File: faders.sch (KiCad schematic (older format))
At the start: 11 parts

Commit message: Sub boards completed
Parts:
- added U6: CD74HC4067M, Package_SO:SOIC-24W_7.5x15.4mm_P1.27mm, symbol 74xx:CD74HC4067M
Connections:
- net +5V: now also U6.24 (VCC)
- net GND: now also U6.12 (GND), U6.15 (~E)
- net F_CHAN_1: no longer names the net of RV1.2, SW_F1.20
- net F_CHAN_1: now also U6.9 (I0)
- net F_CHAN_2: no longer names the net of RV2.2, SW_F1.19
- net F_CHAN_2: now also U6.8 (I1)
- net F_CHAN_3: no longer names the net of RV3.2, SW_F1.18
- net F_CHAN_3: now also U6.7 (I2)
- net F_CHAN_4: no longer names the net of RV4.2, SW_F1.17
- net F_CHAN_4: now also U6.6 (I3)
- net F_CHAN_5: no longer names the net of RV5.2, SW_F1.16
- net F_CHAN_5: now also U6.5 (I4)
- net F_CHAN_6: no longer names the net of RV6.2, SW_F1.15
- net F_CHAN_6: now also U6.4 (I5)
- net F_CHAN_7: no longer names the net of RV7.2, SW_F1.14
- net F_CHAN_7: now also U6.3 (I6)
- net F_CHAN_8: no longer names the net of RV8.2, SW_F1.13
- net F_CHAN_8: now also U6.2 (I7)
- net F_MASTER: no longer names the net of RVM1.2, SW_F1.12
- net F_MASTER: now also U6.23 (I8)
- new net FADERS: U6.1 (COM)
- new net S0: U6.10 (S0)
- new net S1: U6.11 (S1)
- new net S2: U6.14 (S2)
- new net S3: U6.13 (S3)
- no-connect marks 2 -> 9
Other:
- moved on the sheet: RN1, RV1, RV2, RV3, RV4, RV5, RV6, RV7, RV8, RVM1, SW_F1

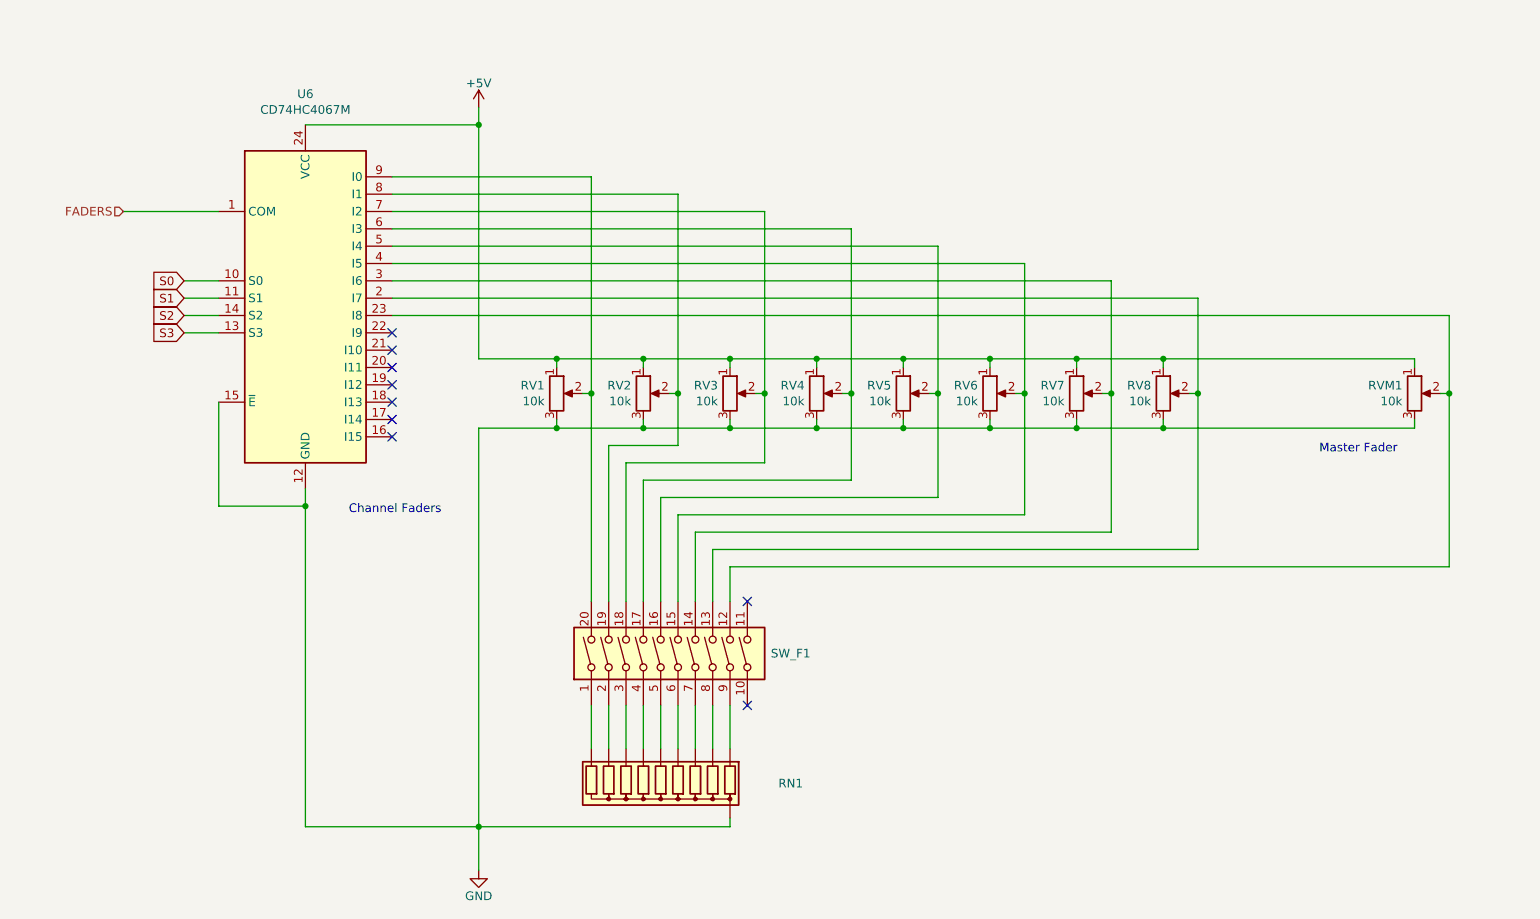
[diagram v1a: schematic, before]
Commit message: Tidy schematic / renumber components / complete daughter boards
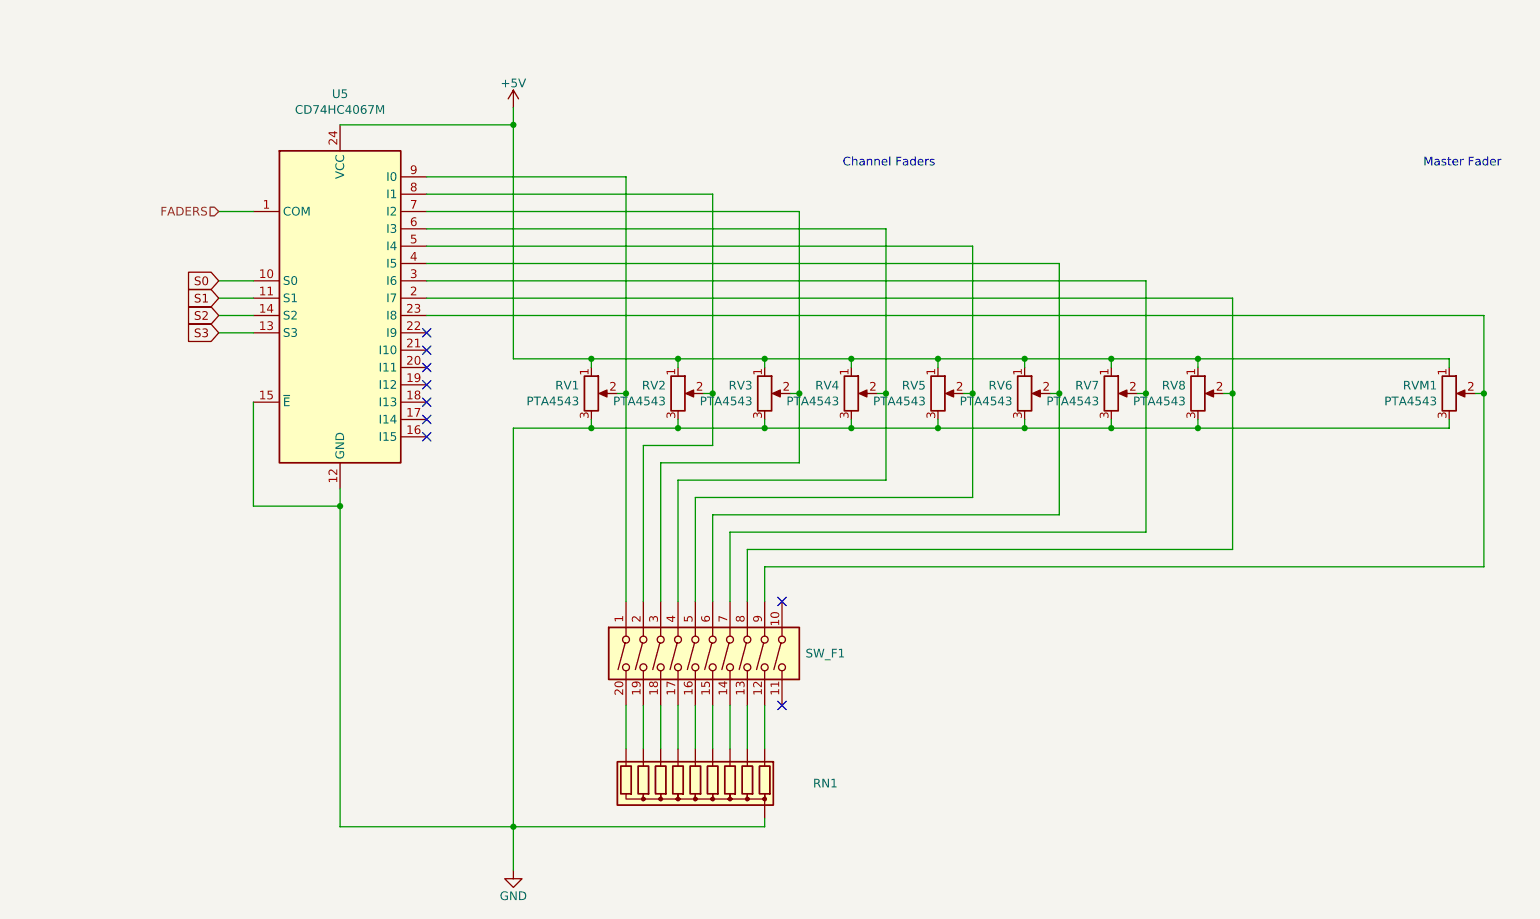
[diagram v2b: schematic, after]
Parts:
- RN1: value R_Network09 -> 2.2K (Bussed)
- RV1, RV2, RV3, RV4, RV5, RV6, RV7, RV8, RVM1: value 10k -> PTA4543
- renumbered U6 to U5
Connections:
- net at SW_F1.1: now also RV1.2, U5.9 (I0); no longer RN1.10 (R9)
- net at RVM1.2, U5.23 (I8): now also SW_F1.9; no longer SW_F1.12
- net at RV8.2, U5.2 (I7): now also SW_F1.8; no longer SW_F1.13
- net at RV7.2, U5.3 (I6): now also SW_F1.7; no longer SW_F1.14
- net at RV6.2, U5.4 (I5): now also SW_F1.6; no longer SW_F1.15
- net at RV5.2, U5.5 (I4): now also SW_F1.5; no longer SW_F1.16
- net at RV4.2, U5.6 (I3): now also SW_F1.4; no longer SW_F1.17
- net at RV3.2, U5.7 (I2): now also SW_F1.3; no longer SW_F1.18
- net at RV2.2, U5.8 (I1): now also SW_F1.2; no longer SW_F1.19
- net at RN1.9 (R8): now also SW_F1.19; no longer SW_F1.2
- net at RN1.8 (R7): now also SW_F1.18; no longer SW_F1.3
- net at RN1.7 (R6): now also SW_F1.17; no longer SW_F1.4
- net at RN1.6 (R5): now also SW_F1.16; no longer SW_F1.5
- net at RN1.5 (R4): now also SW_F1.15; no longer SW_F1.6
- net at RN1.4 (R3): now also SW_F1.14; no longer SW_F1.7
- net at RN1.3 (R2): now also SW_F1.13; no longer SW_F1.8
- net at RN1.2 (R1): now also SW_F1.12; no longer SW_F1.9
- new net: RN1.10 (R9), SW_F1.20
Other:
- moved on the sheet: RN1, RV1, RV2, RV3, RV4, RV5, RV6, RV7, RV8, RVM1, SW_F1, U5

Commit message: Redesign of upper boards
Added bussed resistors following Igor's correction to the schematic + tidied schematic.
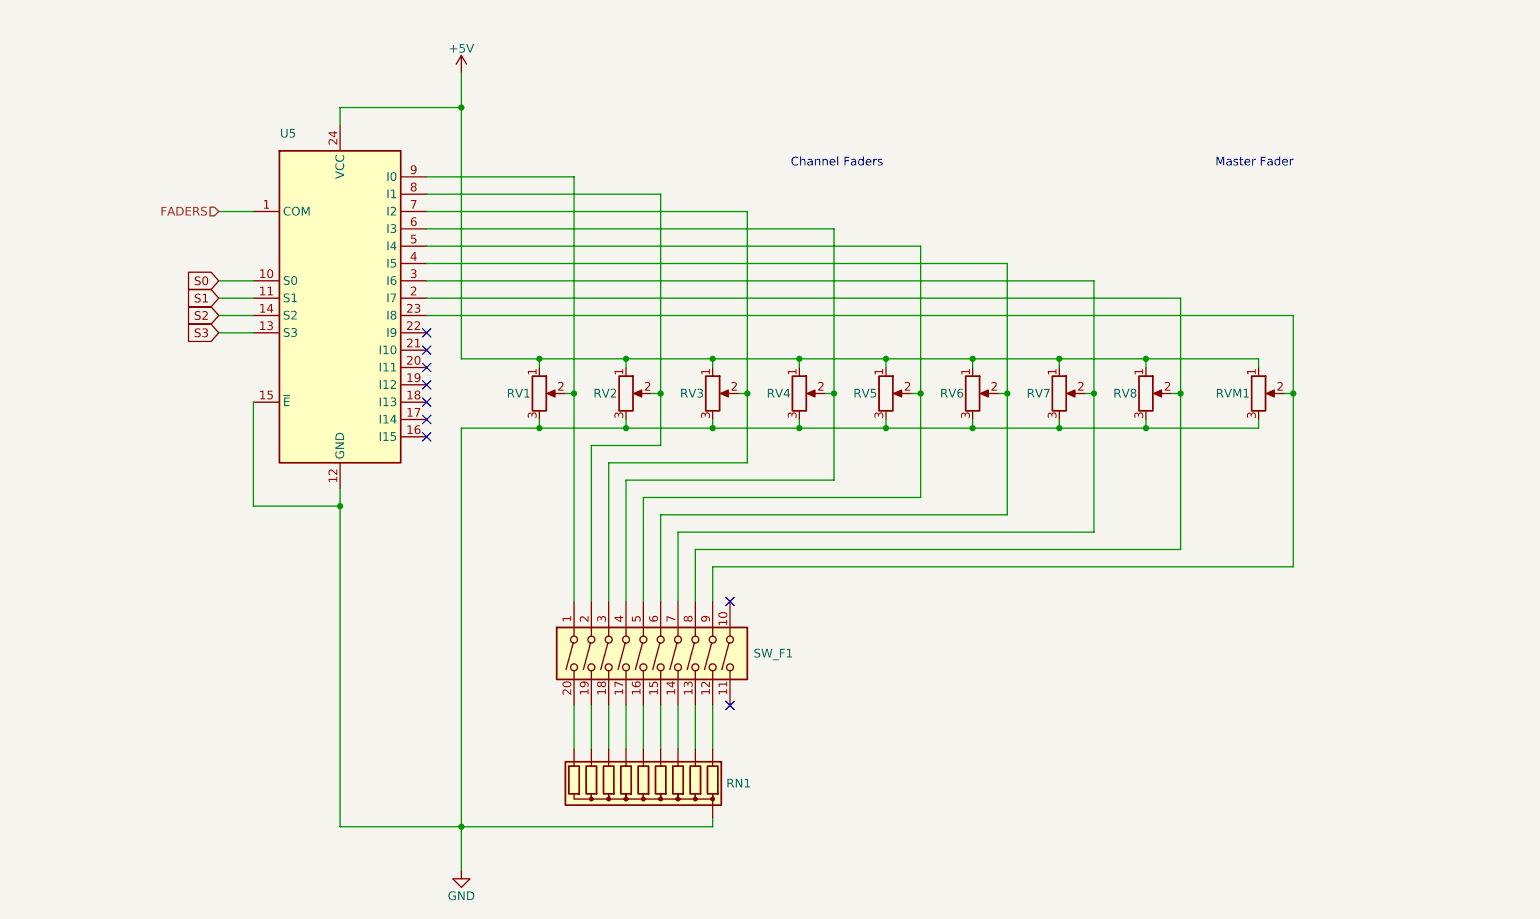
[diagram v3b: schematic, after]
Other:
- moved on the sheet: RN1, RV1, RV2, RV3, RV4, RV5, RV6, RV7, RV8, RVM1, SW_F1

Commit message: Further cleanup and placement
Removed all the connectors to the rails as they're irrelevant to the top boards.

Added all the support headers.

Need to work out the correct routing for the headers but the placement is correct.
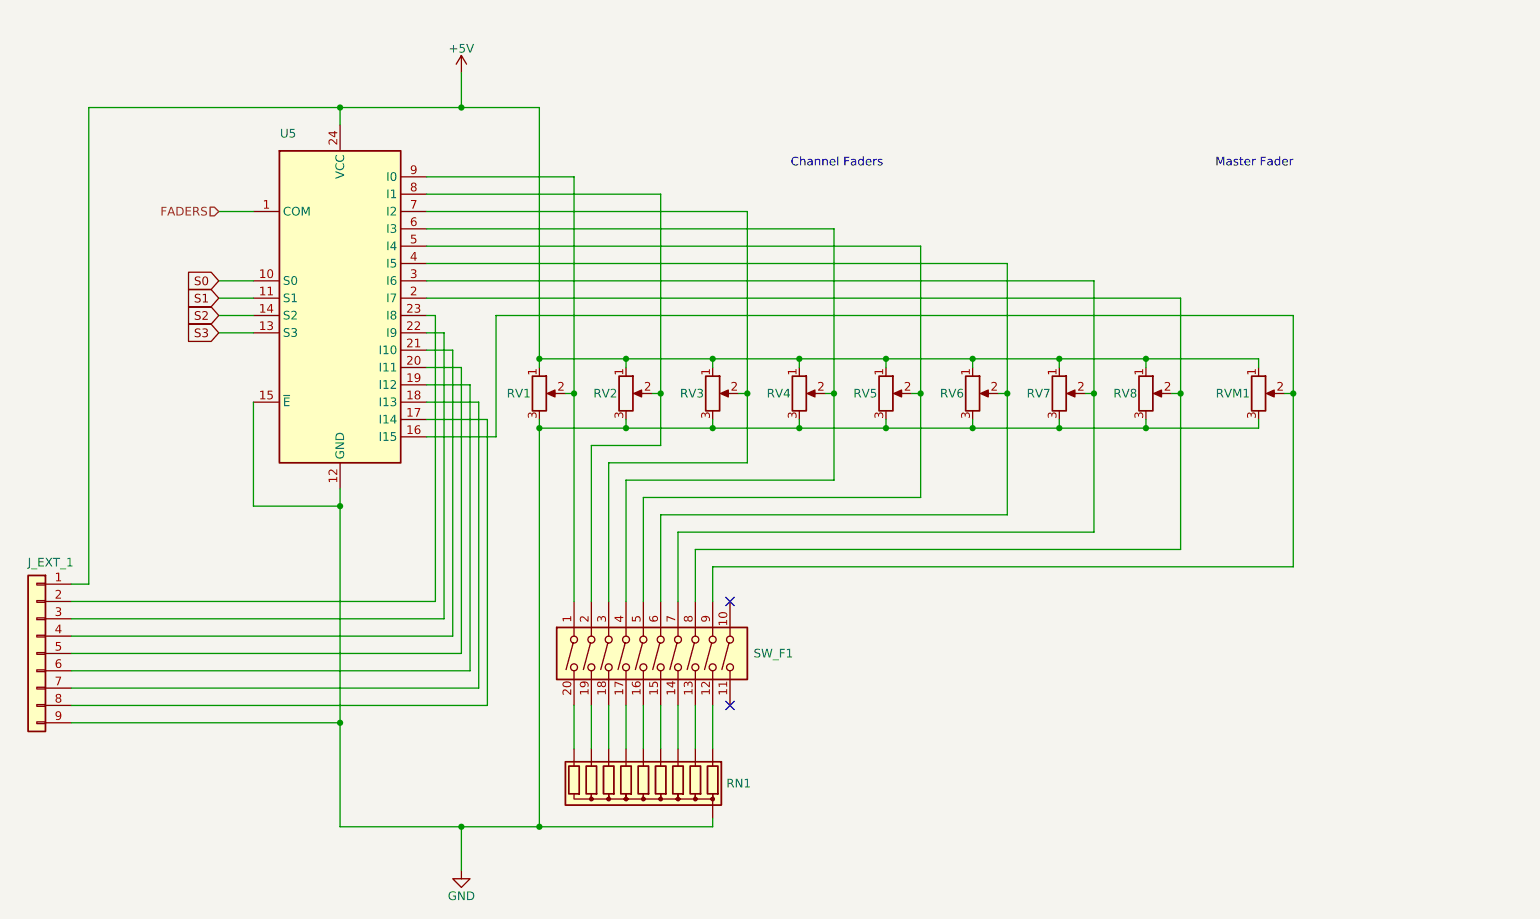
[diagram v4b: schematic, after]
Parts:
- added J_EXT_1: Conn_01x10, Connector_PinSocket_2.54mm:PinSocket_1x09_P2.54mm_Vertical, symbol Connector_Generic:Conn_01x09
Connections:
- net +5V: now also J_EXT_1.1 (Pin_1)
- net GND: now also J_EXT_1.9 (Pin_9)
- net at RVM1.2, SW_F1.9: now also U5.16 (I15); no longer U5.23 (I8)
- net at U5.17 (I14): now also J_EXT_1.8 (Pin_8)
- net at U5.18 (I13): now also J_EXT_1.7 (Pin_7)
- net at U5.19 (I12): now also J_EXT_1.6 (Pin_6)
- net at U5.20 (I11): now also J_EXT_1.5 (Pin_5)
- net at U5.21 (I10): now also J_EXT_1.4 (Pin_4)
- net at U5.22 (I9): now also J_EXT_1.3 (Pin_3)
- new net: J_EXT_1.2 (Pin_2), U5.23 (I8)
- no-connect marks 9 -> 2
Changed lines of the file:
@@
 $Descr A4 11693 8268
 encoding utf-8
-Sheet 2 9
+Sheet 2 8
 Title "cp_midi_controller_002"
 Date "2019-01-13"
-Rev "v1"
+Rev "v3"
 Comp "Cunabula Press"
 Comment1 ""
@@
 	4350 2600 3850 2600
 Connection ~ 4350 2600
-Wire Wire Line
-	3850 3000 3400 3000
-Wire Wire Line
-	3400 3000 3400 5300
 Connection ~ 3850 3000
 Wire Wire Line
 	4850 5250 4850 5300
 Wire Wire Line
-	4850 5300 3400 5300
+	4850 5300 3850 5300
 Connection ~ 3400 5300
 Wire Wire Line
 	3400 5300 3400 5550
-Wire Wire Line
-	3850 2600 3400 2600
 Connection ~ 3850 2600
 Wire Wire Line
@@
 Connection ~ 2700 3450
 Wire Wire Line
-	2700 3450 2700 5300
+	2700 3450 2700 4700
 Wire Wire Line
 	3400 5300 2700 5300
-NoConn ~ 3200 2450
-NoConn ~ 3200 2550
-NoConn ~ 3200 2650
-NoConn ~ 3200 2750
-NoConn ~ 3200 2850
-NoConn ~ 3200 2950
-NoConn ~ 3200 3050
 Text HLabel 2000 1750 0    50   Input ~ 0
 FADERS
@@
 Wire Wire Line
 	2700 1150 3400 1150
-Connection ~ 3400 1150
-Wire Wire Line
-	3400 1150 3400 2600
 Wire Wire Line
 	3400 1150 3400 950
@@
 Wire Wire Line
 	3200 2150 7050 2150
-Wire Wire Line
-	8200 2350 3200 2350
 Wire Wire Line
 	3200 2250 7550 2250
@@
 Wire Wire Line
 	8000 2600 7350 2600
+Wire Wire Line
+	3850 2600 3850 1150
+Wire Wire Line
+	3850 1150 3400 1150
+Connection ~ 3400 1150
+Wire Wire Line
+	3850 3000 3850 5300
+Connection ~ 3850 5300
+Wire Wire Line
+	3850 5300 3400 5300
+$Comp
+L Connector_Generic:Conn_01x09 J_EXT_1
+U 1 1 5D9D211A
+P 950 4300
+F 0 "J_EXT_1" H 870 4825 50  0000 C CNN
+F 1 "Conn_01x10" H 870 4826 50  0001 C CNN
+F 2 "Connector_PinSocket_2.54mm:PinSocket_1x09_P2.54mm_Vertical" H 950 4300 50  0001 C CNN
+F 3 "~" H 950 4300 50  0001 C CNN
+	1    950  4300
+	-1   0    0    -1
+$EndComp
+Wire Wire Line
+	2700 1150 1250 1150
+Wire Wire Line
+	1250 1150 1250 3900
+Wire Wire Line
+	1250 3900 1150 3900
+Connection ~ 2700 1150
+Wire Wire Line
+	1150 4000 3250 4000
+Wire Wire Line
+	1150 4100 3300 4100
+Wire Wire Line
+	3350 4200 1150 4200
+Wire Wire Line
+	3400 4300 1150 4300
+Wire Wire Line
+	1150 4400 3450 4400
+Wire Wire Line
+	3500 4500 1150 4500
+Wire Wire Line
+	3550 4600 1150 4600
+Wire Wire Line
+	1150 4700 2700 4700
+Connection ~ 2700 4700
+Wire Wire Line
+	2700 4700 2700 5300
+Wire Wire Line
+	3200 3050 3550 3050
+Wire Wire Line
+	3600 2350 3600 3050
+Wire Wire Line
+	3600 3050 3550 3050
+Wire Wire Line
+	3600 2350 8200 2350
+Wire Wire Line
+	3550 2950 3550 4600
+Wire Wire Line
+	3200 2350 3250 2350
+Wire Wire Line
+	3250 2350 3250 4000
+Wire Wire Line
+	3200 2450 3300 2450
+Wire Wire Line
+	3300 2450 3300 4100
+Wire Wire Line
+	3200 2550 3350 2550
+Wire Wire Line
+	3350 2550 3350 4200
+Wire Wire Line
+	3200 2650 3400 2650
+Wire Wire Line
+	3400 2650 3400 4300
+Wire Wire Line
+	3200 2750 3450 2750
+Wire Wire Line
+	3450 2750 3450 4400
+Wire Wire Line
+	3200 2850 3500 2850
+Wire Wire Line
+	3500 2850 3500 4500
+Wire Wire Line
+	3550 2950 3200 2950
 $EndSCHEMATC

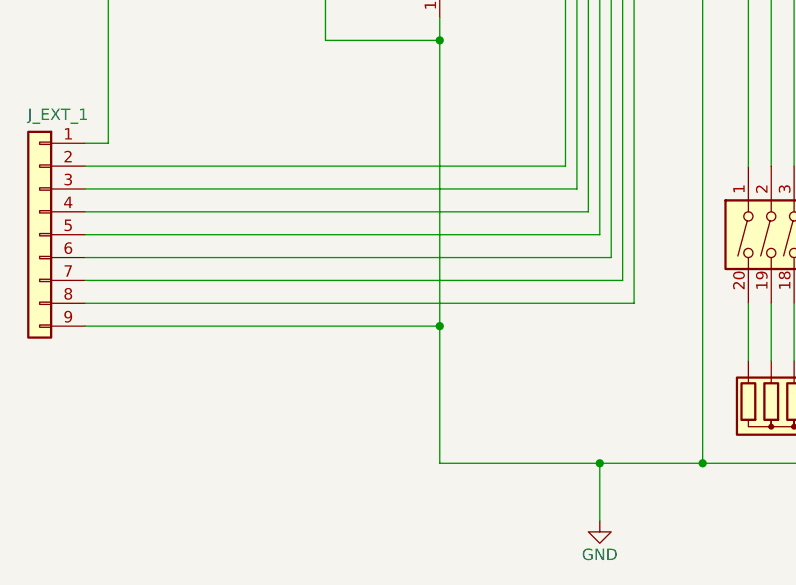
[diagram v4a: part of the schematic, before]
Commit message: Added external connections / removed unused
+18 Buttons
+ Different connections for 7 spare multiplexer slots
- Unused Arduino pins
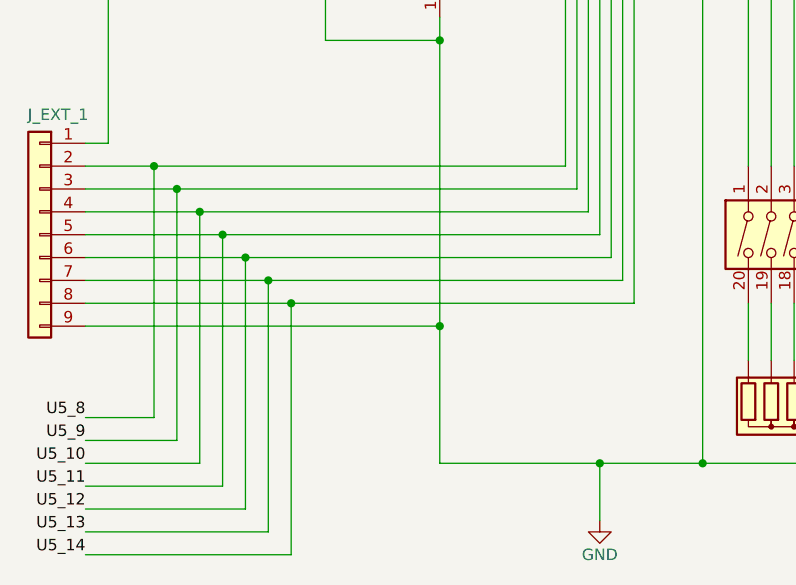
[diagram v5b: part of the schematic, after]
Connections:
- net U5_14: now reaches J_EXT_1.8 (Pin_8), U5.17 (I14)
- net U5_13: now reaches J_EXT_1.7 (Pin_7), U5.18 (I13)
- net U5_12: now reaches J_EXT_1.6 (Pin_6), U5.19 (I12)
- net U5_11: now reaches J_EXT_1.5 (Pin_5), U5.20 (I11)
- net U5_10: now reaches J_EXT_1.4 (Pin_4), U5.21 (I10)
- net U5_9: now reaches J_EXT_1.3 (Pin_3), U5.22 (I9)
- net U5_8: now reaches J_EXT_1.2 (Pin_2), U5.23 (I8)
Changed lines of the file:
@@
 Connection ~ 2700 1150
 Wire Wire Line
-	1150 4000 3250 4000
+	1150 4100 1550 4100
 Wire Wire Line
-	1150 4100 3300 4100
+	3350 4200 1650 4200
 Wire Wire Line
-	3350 4200 1150 4200
+	3400 4300 1750 4300
 Wire Wire Line
-	3400 4300 1150 4300
+	1150 4400 1850 4400
 Wire Wire Line
-	1150 4400 3450 4400
+	3500 4500 1950 4500
 Wire Wire Line
-	3500 4500 1150 4500
-Wire Wire Line
-	3550 4600 1150 4600
+	3550 4600 2050 4600
 Wire Wire Line
 	1150 4700 2700 4700
@@
 Wire Wire Line
 	3550 2950 3200 2950
+Wire Wire Line
+	1550 4100 1550 5200
+Wire Wire Line
+	1550 5200 1150 5200
+Connection ~ 1550 4100
+Wire Wire Line
+	1550 4100 3300 4100
+Wire Wire Line
+	1650 4200 1650 5300
+Wire Wire Line
+	1650 5300 1150 5300
+Connection ~ 1650 4200
+Wire Wire Line
+	1650 4200 1150 4200
+Wire Wire Line
+	1750 4300 1750 5400
+Wire Wire Line
+	1750 5400 1150 5400
+Connection ~ 1750 4300
+Wire Wire Line
+	1750 4300 1150 4300
+Wire Wire Line
+	1150 4000 1450 4000
+Wire Wire Line
+	1450 4000 1450 5100
+Wire Wire Line
+	1150 5100 1450 5100
+Connection ~ 1450 4000
+Wire Wire Line
+	1450 4000 3250 4000
+Wire Wire Line
+	1850 4400 1850 5500
+Wire Wire Line
+	1850 5500 1150 5500
+Connection ~ 1850 4400
+Wire Wire Line
+	1850 4400 3450 4400
+Wire Wire Line
+	1950 4500 1950 5600
+Wire Wire Line
+	1950 5600 1150 5600
+Connection ~ 1950 4500
+Wire Wire Line
+	1950 4500 1150 4500
+Wire Wire Line
+	2050 4600 2050 5700
+Wire Wire Line
+	2050 5700 1150 5700
+Connection ~ 2050 4600
+Wire Wire Line
+	2050 4600 1150 4600
+Text Label 1150 5100 2    50   ~ 0
+U5_8
+Text Label 1150 5200 2    50   ~ 0
+U5_9
+Text Label 1150 5300 2    50   ~ 0
+U5_10
+Text Label 1150 5400 2    50   ~ 0
+U5_11
+Text Label 1150 5500 2    50   ~ 0
+U5_12
+Text Label 1150 5600 2    50   ~ 0
+U5_13
+Text Label 1150 5700 2    50   ~ 0
+U5_14
 $EndSCHEMATC
